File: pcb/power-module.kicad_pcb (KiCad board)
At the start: 4 copper layers, 55 x 55 mm, 53 parts, among them J1 USB_C_PowerOnly_6P, J2 Power, U1 AZ1084-3.3, U2 LM66200DRLR

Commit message: Added tag to pcb to capture version on release; updated check in script to fill in tag
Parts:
- removed kibuzzard-67F873E4: G***, kibuzzard-67F873E4
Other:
- board text added: "<<tag>>"

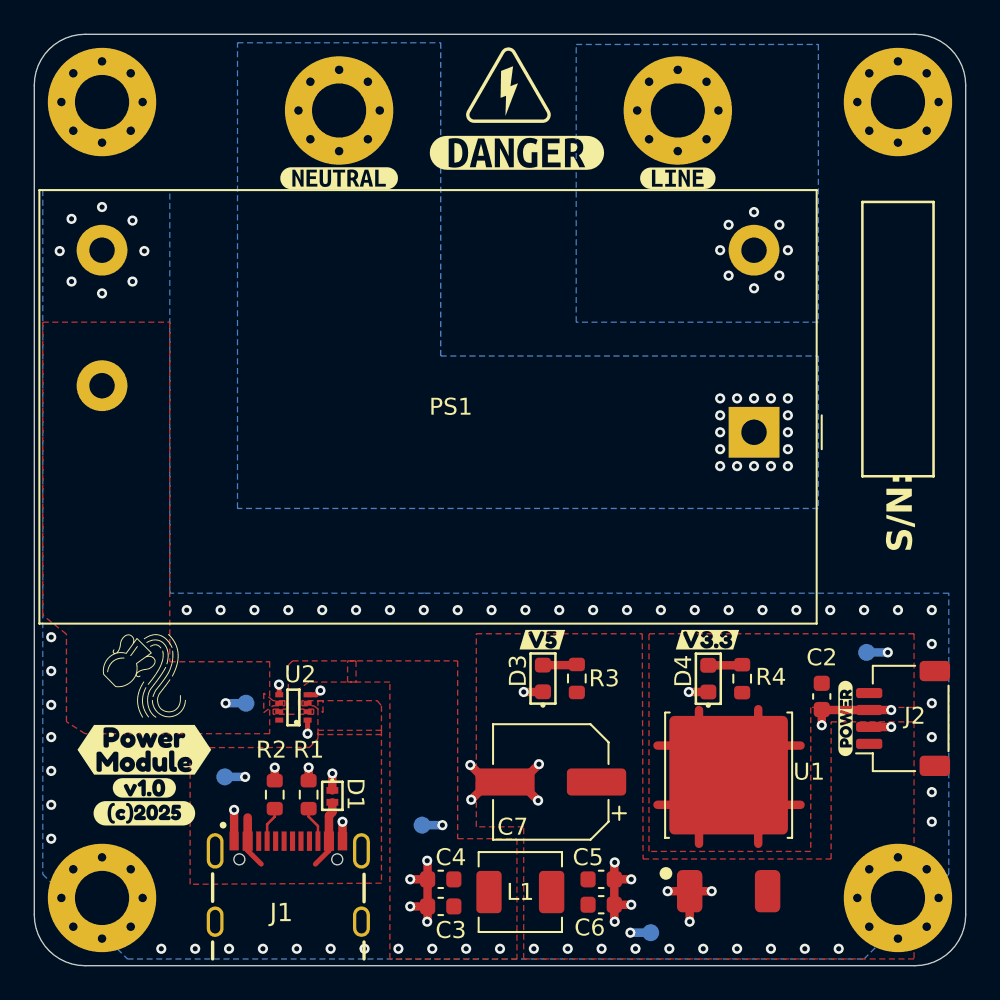
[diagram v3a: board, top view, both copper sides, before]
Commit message: Separated 22uF into two 10uF; rerouted everything for better layout
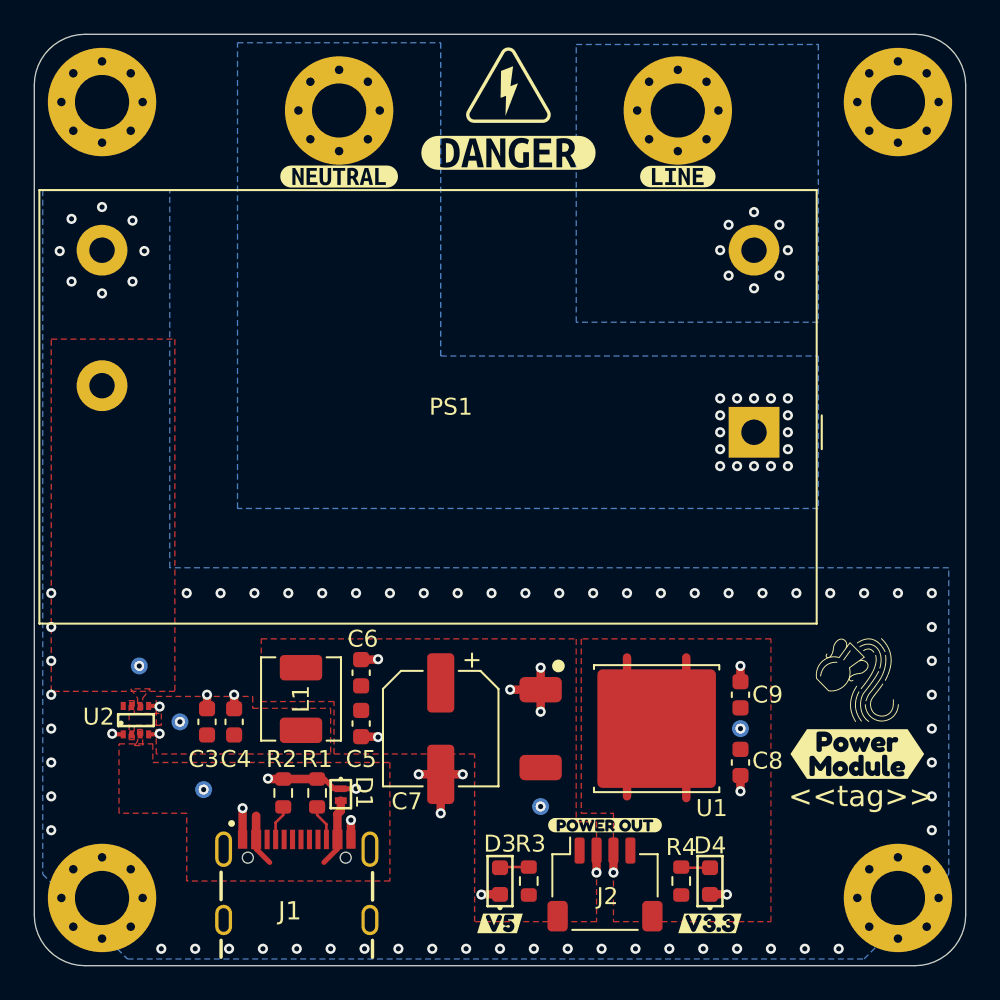
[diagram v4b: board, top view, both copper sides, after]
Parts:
- removed C2: 22uF, Capacitor_SMD:C_0603_1608Metric
- removed kibuzzard-67E31E9F: G***, kibuzzard-67E31E9F
- removed kibuzzard-681BE833: G***, kibuzzard-681BE833
- removed kibuzzard-681CF8FE: G***, kibuzzard-681CF8FE
- added C8: 10uF, Capacitor_SMD:C_0603_1608Metric, F.Cu at (91.7, 153.0)
- added C9: 10uF, Capacitor_SMD:C_0603_1608Metric, F.Cu at (91.7, 149.0)
- added kibuzzard-683B0AC2: G***, kibuzzard-683B0AC2, F.Cu at (83.7, 156.7)
- moved LOGO4 42.1 mm to (98.5, 150.8)
- moved kibuzzard-681CF78D 42.1 mm to (98.6, 152.5)
- moved J2 20.1 mm to (83.7, 160.2), turned to 0 degrees
- moved C6 19.7 mm to (69.3, 147.7), turned to 90 degrees
- moved C3 17.6 mm to (60.2, 150.6), turned to 90 degrees
- moved L1 17.3 mm to (65.8, 149.2), turned to 90 degrees
- moved kibuzzard-6823F461 16.9 mm to (77.5, 162.5)
- moved C5 16.9 mm to (69.3, 150.7), turned to -90 degrees
- moved kibuzzard-6823F476 16.8 mm to (89.9, 162.5)
- moved TP2 15.5 mm to (58.6, 150.6)
- moved C4 15.3 mm to (61.8, 150.6), turned to 90 degrees
- moved R4 12.5 mm to (88.2, 160.0)
- moved R3 12.3 mm to (79.2, 160.0)
- moved D3 12.2 mm to (77.5, 160.0)
- moved kibuzzard-68104292 12.2 mm to (82.1, 155.6)
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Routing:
- net GND: track 42.1 -> 30.1 mm, vias 92 -> 90
- net +3.3V: track 20.0 -> 9.50 mm
- net LINE_5V: track 1.20 -> 0.00 mm
- net +5V: track 1.20 -> 0.00 mm
- net RAW_5V: track 1.20 -> 0.00 mm
- net USB_5V: track 8.48 -> 7.28 mm
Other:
- board text removed: "S/N:"
